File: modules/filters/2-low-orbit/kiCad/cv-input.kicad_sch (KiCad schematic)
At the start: 23 parts, among them Q1 BC548, U2 TL074

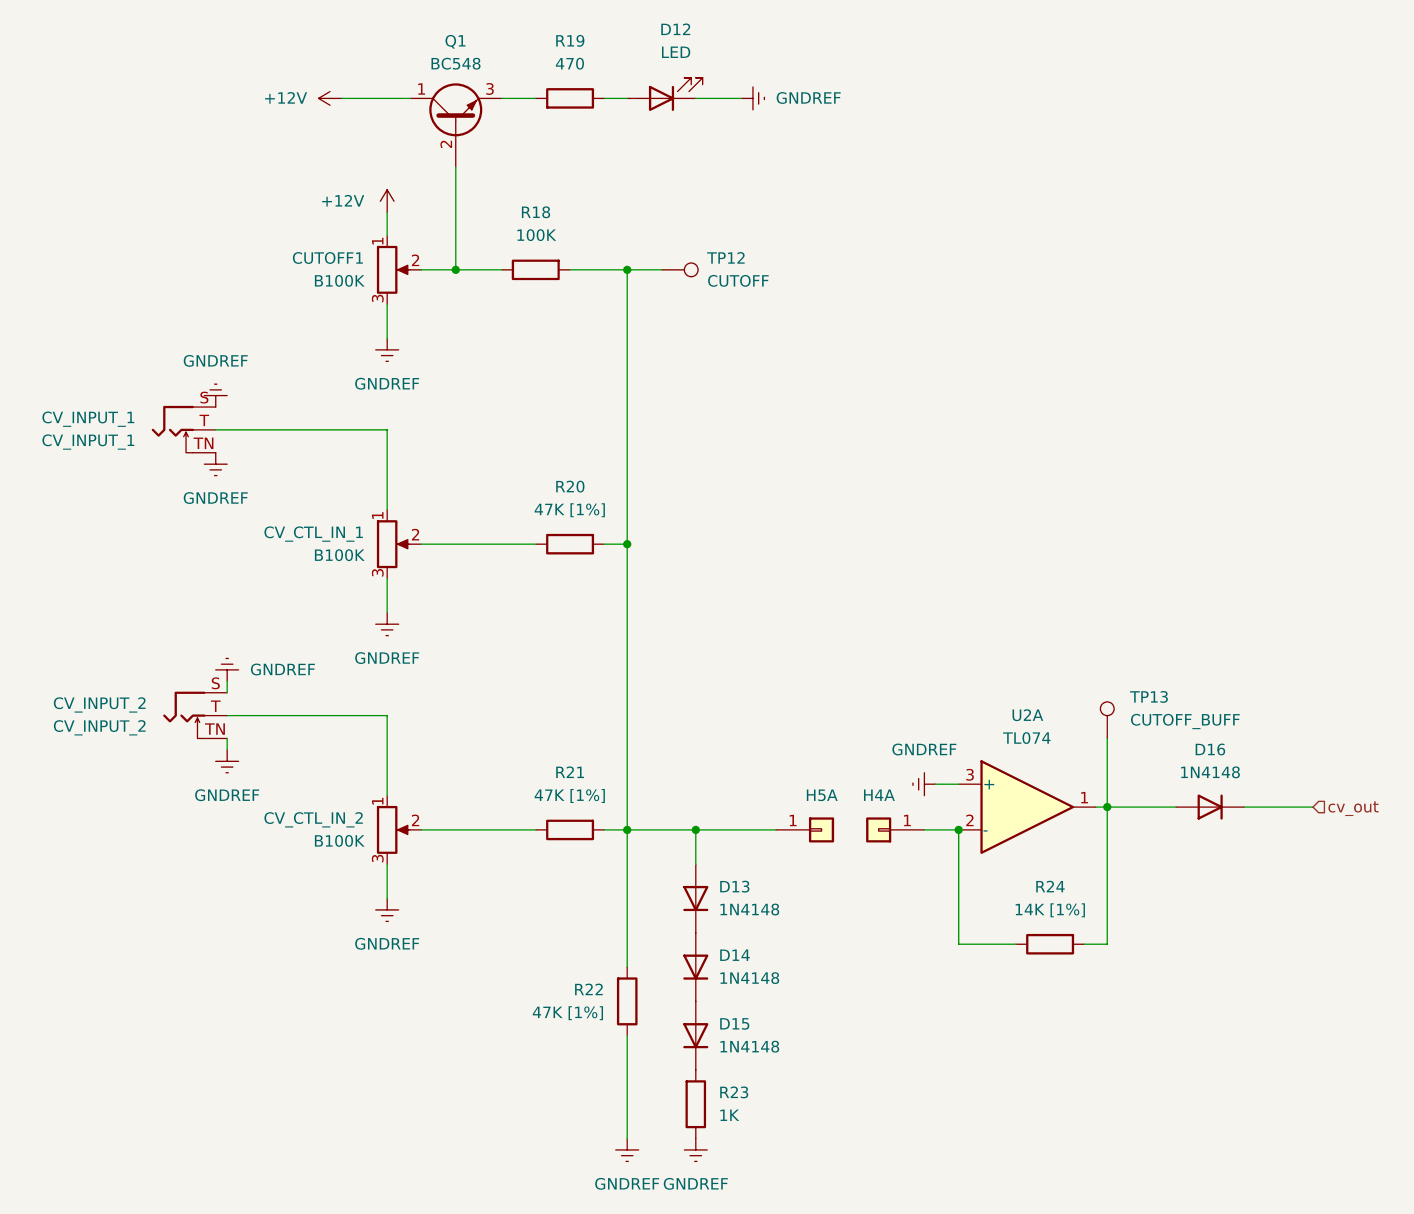
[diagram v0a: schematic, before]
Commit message: update component status, add IBOM for built modules
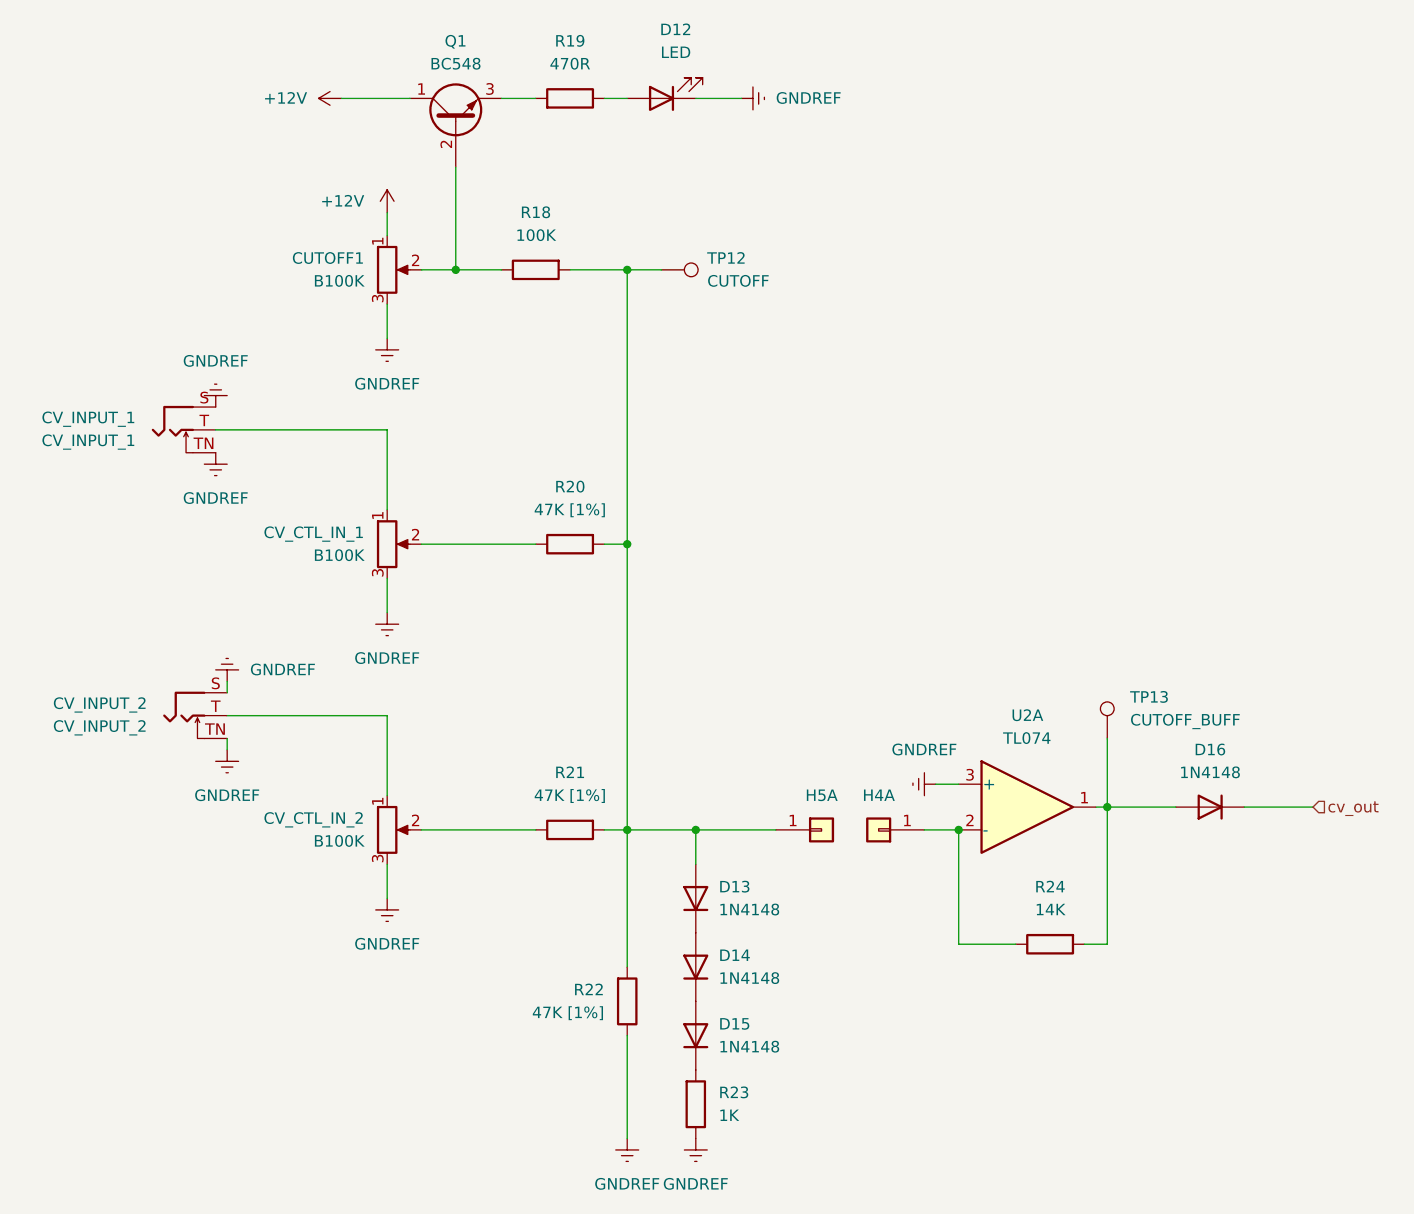
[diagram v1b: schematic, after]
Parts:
- H4: value BTM_4_SGL -> PinSocket_01x04
- H5: value TOP_4_SGL -> PinHeader_01x04
- R19: value 470 -> 470R
- R24: value 14K [1%] -> 14K
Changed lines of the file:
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@@
 			)
 		)
-		(property "Value" "BTM_4_SGL"
+		(property "Value" "PinSocket_01x04"
 			(at 156.21 119.38 0)
 			(effects
@@
 			)
 		)
-		(property "Value" "TOP_4_SGL"
+		(property "Value" "PinHeader_01x04"
 			(at 149.86 114.3 0)
 			(effects
@@
 			)
 		)
-		(property "Value" "470"
+		(property "Value" "470R"
 			(at 121.92 31.75 90)
 			(effects
@@
 			)
 		)
-		(property "Value" "14K [1%]"
+		(property "Value" "14K"
 			(at 175.26 125.73 90)
 			(effects
